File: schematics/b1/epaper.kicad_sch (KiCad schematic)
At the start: 11 parts

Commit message: Updated dates.
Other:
- title: B1 -> E-Paper
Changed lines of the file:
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@@
   (paper "A5")
   (title_block
-    (title "B1")
-    (date "2024-02-15")
+    (title "E-Paper")
+    (date "2024-02-19")
     (rev "1")
     (company "shawnd.xyz")

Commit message: Updated annotations.
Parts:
- renumbered TP48 to TP47, TP51 to TP48, TP50 to TP49, TP49 to TP50, TP47 to TP51, U6 to U8
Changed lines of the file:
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@@
   (symbol (lib_id "power:GND") (at 58.42 45.72 0) (unit 1)
     (in_bom yes) (on_board yes) (dnp no) (fields_autoplaced)
-    (property "Reference" "#PWR040" (at 58.42 52.07 0)
+    (property "Reference" "#PWR039" (at 58.42 52.07 0)
       (effects (font (size 1.27 1.27)) hide)
     )
@@
       (project "b1"
         (path "/d6142fa5-2354-4512-9919-37616259c364/793d8791-3733-41a0-9e62-38f7f458300f"
-          (reference "#PWR040") (unit 1)
+          (reference "#PWR039") (unit 1)
         )
       )
@@
   (symbol (lib_id "Connector:TestPoint") (at 74.93 76.2 180) (unit 1)
     (in_bom yes) (on_board yes) (dnp no)
-    (property "Reference" "TP51" (at 73.66 81.28 90)
+    (property "Reference" "TP48" (at 74.93 81.28 90)
       (effects (font (size 1.27 1.27)) (justify left))
     )
     (property "Value" "TestPoint" (at 76.2 81.28 90)
-      (effects (font (size 1.27 1.27)) (justify left))
+      (effects (font (size 1.27 1.27)) (justify left) hide)
     )
     (property "Footprint" "" (at 69.85 76.2 0)
@@
       (project "b1"
         (path "/d6142fa5-2354-4512-9919-37616259c364/793d8791-3733-41a0-9e62-38f7f458300f"
+          (reference "TP48") (unit 1)
+        )
+      )
+    )
+  )
+  (symbol (lib_id "Connector:TestPoint") (at 87.63 76.2 180) (unit 1)
+    (in_bom yes) (on_board yes) (dnp no)
+    (property "Reference" "TP50" (at 87.63 81.28 90)
+      (effects (font (size 1.27 1.27)) (justify left))
+    )
+    (property "Value" "TestPoint" (at 88.9 81.28 90)
+      (effects (font (size 1.27 1.27)) (justify left) hide)
+    )
+    (property "Footprint" "" (at 82.55 76.2 0)
+      (effects (font (size 1.27 1.27)) hide)
+    )
+    (property "Datasheet" "~" (at 82.55 76.2 0)
+      (effects (font (size 1.27 1.27)) hide)
+    )
+    (pin "1")
+    (instances
+      (project "b1"
+        (path "/d6142fa5-2354-4512-9919-37616259c364/793d8791-3733-41a0-9e62-38f7f458300f"
+          (reference "TP50") (unit 1)
+        )
+      )
+    )
+  )
+  (symbol (lib_id "Connector:TestPoint") (at 105.41 77.47 270) (unit 1)
+    (in_bom yes) (on_board yes) (dnp no)
+    (property "Reference" "TP51" (at 110.49 77.47 90)
+      (effects (font (size 1.27 1.27)) (justify left))
+    )
+    (property "Value" "TestPoint" (at 110.49 78.74 90)
+      (effects (font (size 1.27 1.27)) (justify left) hide)
+    )
+    (property "Footprint" "" (at 105.41 82.55 0)
+      (effects (font (size 1.27 1.27)) hide)
+    )
+    (property "Datasheet" "~" (at 105.41 82.55 0)
+      (effects (font (size 1.27 1.27)) hide)
+    )
+    (pin "1")
+    (instances
+      (project "b1"
+        (path "/d6142fa5-2354-4512-9919-37616259c364/793d8791-3733-41a0-9e62-38f7f458300f"
           (reference "TP51") (unit 1)
         )
@@
     )
   )
-  (symbol (lib_id "Connector:TestPoint") (at 87.63 76.2 180) (unit 1)
-    (in_bom yes) (on_board yes) (dnp no)
-    (property "Reference" "TP49" (at 86.36 81.28 90)
-      (effects (font (size 1.27 1.27)) (justify left))
-    )
-    (property "Value" "TestPoint" (at 88.9 81.28 90)
-      (effects (font (size 1.27 1.27)) (justify left))
-    )
-    (property "Footprint" "" (at 82.55 76.2 0)
-      (effects (font (size 1.27 1.27)) hide)
-    )
-    (property "Datasheet" "~" (at 82.55 76.2 0)
-      (effects (font (size 1.27 1.27)) hide)
-    )
-    (pin "1")
-    (instances
-      (project "b1"
-        (path "/d6142fa5-2354-4512-9919-37616259c364/793d8791-3733-41a0-9e62-38f7f458300f"
-          (reference "TP49") (unit 1)
-        )
-      )
-    )
-  )
-  (symbol (lib_id "Connector:TestPoint") (at 105.41 77.47 270) (unit 1)
-    (in_bom yes) (on_board yes) (dnp no) (fields_autoplaced)
-    (property "Reference" "TP47" (at 110.49 76.2 90)
-      (effects (font (size 1.27 1.27)) (justify left))
-    )
-    (property "Value" "TestPoint" (at 110.49 78.74 90)
-      (effects (font (size 1.27 1.27)) (justify left))
-    )
-    (property "Footprint" "" (at 105.41 82.55 0)
-      (effects (font (size 1.27 1.27)) hide)
-    )
-    (property "Datasheet" "~" (at 105.41 82.55 0)
+  (symbol (lib_id "Connector:TestPoint") (at 121.92 59.69 180) (unit 1)
+    (in_bom yes) (on_board yes) (dnp no)
+    (property "Reference" "TP47" (at 121.92 64.77 90)
+      (effects (font (size 1.27 1.27)) (justify left))
+    )
+    (property "Value" "TestPoint" (at 123.19 64.77 90)
+      (effects (font (size 1.27 1.27)) (justify left) hide)
+    )
+    (property "Footprint" "" (at 116.84 59.69 0)
+      (effects (font (size 1.27 1.27)) hide)
+    )
+    (property "Datasheet" "~" (at 116.84 59.69 0)
       (effects (font (size 1.27 1.27)) hide)
     )
@@
         (path "/d6142fa5-2354-4512-9919-37616259c364/793d8791-3733-41a0-9e62-38f7f458300f"
           (reference "TP47") (unit 1)
-        )
-      )
-    )
-  )
-  (symbol (lib_id "Connector:TestPoint") (at 121.92 59.69 180) (unit 1)
-    (in_bom yes) (on_board yes) (dnp no)
-    (property "Reference" "TP48" (at 120.65 64.77 90)
-      (effects (font (size 1.27 1.27)) (justify left))
-    )
-    (property "Value" "TestPoint" (at 123.19 64.77 90)
-      (effects (font (size 1.27 1.27)) (justify left))
-    )
-    (property "Footprint" "" (at 116.84 59.69 0)
-      (effects (font (size 1.27 1.27)) hide)
-    )
-    (property "Datasheet" "~" (at 116.84 59.69 0)
-      (effects (font (size 1.27 1.27)) hide)
-    )
-    (pin "1")
-    (instances
-      (project "b1"
-        (path "/d6142fa5-2354-4512-9919-37616259c364/793d8791-3733-41a0-9e62-38f7f458300f"
-          (reference "TP48") (unit 1)
         )
       )
@@
   (symbol (lib_id "power:GND") (at 104.14 78.74 0) (unit 1)
     (in_bom yes) (on_board yes) (dnp no) (fields_autoplaced)
-    (property "Reference" "#PWR021" (at 104.14 85.09 0)
+    (property "Reference" "#PWR040" (at 104.14 85.09 0)
       (effects (font (size 1.27 1.27)) hide)
     )
@@
       (project "b1"
         (path "/d6142fa5-2354-4512-9919-37616259c364/793d8791-3733-41a0-9e62-38f7f458300f"
-          (reference "#PWR021") (unit 1)
+          (reference "#PWR040") (unit 1)
         )
       )
@@
   (symbol (lib_id "custom:E-paper_Display") (at 104.14 58.42 0) (unit 1)
     (in_bom yes) (on_board yes) (dnp no)
-    (property "Reference" "U6" (at 106.68 49.53 0)
+    (property "Reference" "U8" (at 106.68 49.53 0)
       (effects (font (size 1.27 1.27)))
     )
@@
       (project "b1"
         (path "/d6142fa5-2354-4512-9919-37616259c364/793d8791-3733-41a0-9e62-38f7f458300f"
-          (reference "U6") (unit 1)
+          (reference "U8") (unit 1)
         )
       )
@@
   )
   (symbol (lib_id "Connector:TestPoint") (at 105.41 41.91 270) (unit 1)
-    (in_bom yes) (on_board yes) (dnp no) (fields_autoplaced)
-    (property "Reference" "TP46" (at 110.49 40.64 90)
+    (in_bom yes) (on_board yes) (dnp no)
+    (property "Reference" "TP46" (at 110.49 41.91 90)
       (effects (font (size 1.27 1.27)) (justify left))
     )
     (property "Value" "TestPoint" (at 110.49 43.18 90)
-      (effects (font (size 1.27 1.27)) (justify left))
+      (effects (font (size 1.27 1.27)) (justify left) hide)
     )
     (property "Footprint" "" (at 105.41 46.99 0)
@@
   (symbol (lib_id "Connector:TestPoint") (at 81.28 76.2 180) (unit 1)
     (in_bom yes) (on_board yes) (dnp no)
-    (property "Reference" "TP50" (at 80.01 81.28 90)
+    (property "Reference" "TP49" (at 81.28 81.28 90)
       (effects (font (size 1.27 1.27)) (justify left))
     )
     (property "Value" "TestPoint" (at 82.55 81.28 90)
-      (effects (font (size 1.27 1.27)) (justify left))
+      (effects (font (size 1.27 1.27)) (justify left) hide)
     )
     (property "Footprint" "" (at 76.2 76.2 0)
@@
       (project "b1"
         (path "/d6142fa5-2354-4512-9919-37616259c364/793d8791-3733-41a0-9e62-38f7f458300f"
-          (reference "TP50") (unit 1)
-        )
-      )
+          (reference "TP49") (unit 1)
+        )
+      )

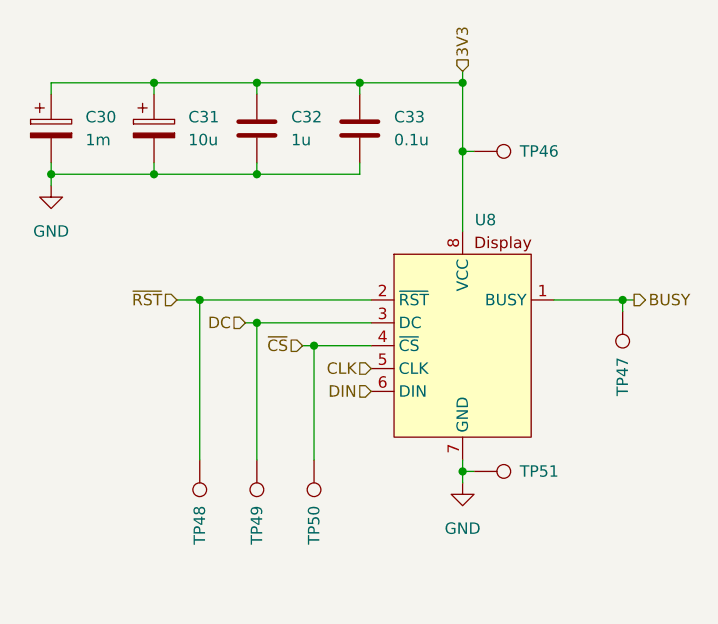
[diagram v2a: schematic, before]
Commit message: Tweaked wiring.
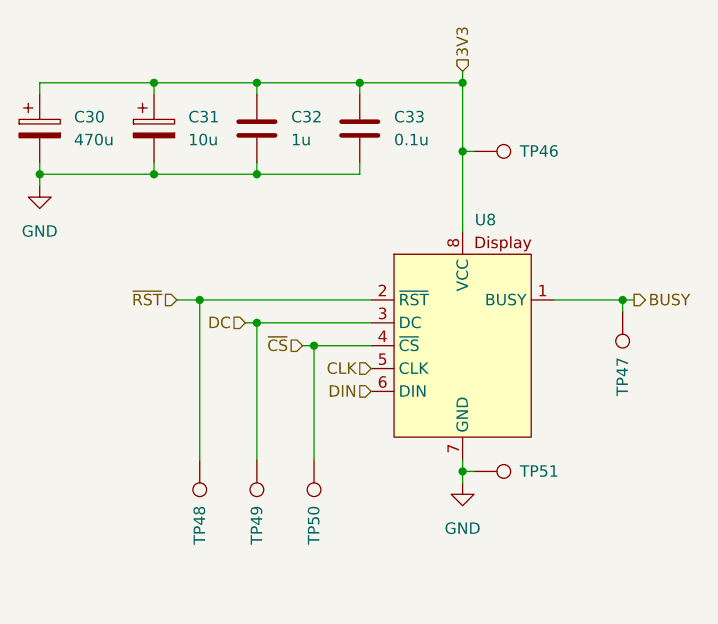
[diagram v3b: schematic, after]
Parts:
- C30: value 1m -> 470u
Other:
- moved on the sheet: C30
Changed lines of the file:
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@@
   (junction (at 104.14 77.47) (diameter 0) (color 0 0 0 0)
   )
-  (junction (at 58.42 44.45) (diameter 0) (color 0 0 0 0)
-  )
   (junction (at 104.14 34.29) (diameter 0) (color 0 0 0 0)
   )
+  (junction (at 57.15 44.45) (diameter 0) (color 0 0 0 0)
+  )
   (junction (at 69.85 34.29) (diameter 0) (color 0 0 0 0)
   )
@@
     (stroke (width 0) (type default))
   )
-  (wire (pts (xy 58.42 34.29) (xy 69.85 34.29))
+  (wire (pts (xy 57.15 34.29) (xy 69.85 34.29))
     (stroke (width 0) (type default))
   )
@@
     (stroke (width 0) (type default))
   )
-  (wire (pts (xy 58.42 45.72) (xy 58.42 44.45))
+  (wire (pts (xy 57.15 45.72) (xy 57.15 44.45))
     (stroke (width 0) (type default))
   )
@@
     (stroke (width 0) (type default))
   )
-  (wire (pts (xy 58.42 35.56) (xy 58.42 34.29))
+  (wire (pts (xy 57.15 35.56) (xy 57.15 34.29))
     (stroke (width 0) (type default))
   )
@@
     (stroke (width 0) (type default))
   )
-  (wire (pts (xy 58.42 44.45) (xy 69.85 44.45))
+  (wire (pts (xy 57.15 44.45) (xy 69.85 44.45))
     (stroke (width 0) (type default))
   )
@@
     (stroke (width 0) (type default))
   )
-  (wire (pts (xy 58.42 43.18) (xy 58.42 44.45))
+  (wire (pts (xy 57.15 43.18) (xy 57.15 44.45))
     (stroke (width 0) (type default))
   )
@@
     (effects (font (size 1.27 1.27)) (justify left))
   )
-  (symbol (lib_id "power:GND") (at 58.42 45.72 0) (unit 1)
+  (symbol (lib_id "power:GND") (at 57.15 45.72 0) (unit 1)
     (in_bom yes) (on_board yes) (dnp no) (fields_autoplaced)
-    (property "Reference" "#PWR039" (at 58.42 52.07 0)
-      (effects (font (size 1.27 1.27)) hide)
-    )
-    (property "Value" "GND" (at 58.42 50.8 0)
+    (property "Reference" "#PWR039" (at 57.15 52.07 0)
+      (effects (font (size 1.27 1.27)) hide)
+    )
+    (property "Value" "GND" (at 57.15 50.8 0)
       (effects (font (size 1.27 1.27)))
     )
-    (property "Footprint" "" (at 58.42 45.72 0)
-      (effects (font (size 1.27 1.27)) hide)
-    )
-    (property "Datasheet" "" (at 58.42 45.72 0)
+    (property "Footprint" "" (at 57.15 45.72 0)
+      (effects (font (size 1.27 1.27)) hide)
+    )
+    (property "Datasheet" "" (at 57.15 45.72 0)
       (effects (font (size 1.27 1.27)) hide)
     )
@@
     )
   )
-  (symbol (lib_id "Device:C_Polarized") (at 58.42 39.37 0) (unit 1)
-    (in_bom yes) (on_board yes) (dnp no)
-    (property "Reference" "C30" (at 62.23 38.1 0)
-      (effects (font (size 1.27 1.27)) (justify left))
-    )
-    (property "Value" "1m" (at 62.23 40.64 0)
-      (effects (font (size 1.27 1.27)) (justify left))
-    )
-    (property "Footprint" "" (at 59.3852 43.18 0)
-      (effects (font (size 1.27 1.27)) hide)
-    )
-    (property "Datasheet" "~" (at 58.42 39.37 0)
-      (effects (font (size 1.27 1.27)) hide)
-    )
+  (symbol (lib_id "Device:C_Polarized") (at 57.15 39.37 0) (unit 1)
+    (in_bom yes) (on_board yes) (dnp no)
+    (property "Reference" "C30" (at 60.96 38.1 0)
+      (effects (font (size 1.27 1.27)) (justify left))
+    )
+    (property "Value" "470u" (at 60.96 40.64 0)
+      (effects (font (size 1.27 1.27)) (justify left))
+    )
+    (property "Footprint" "" (at 58.1152 43.18 0)
+      (effects (font (size 1.27 1.27)) hide)
+    )
+    (property "Datasheet" "~" (at 57.15 39.37 0)
+      (effects (font (size 1.27 1.27)) hide)
+    )

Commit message: Assigned some footprints.
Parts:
- C30: footprint (none) -> Capacitor_THT:CP_Radial_D8.0mm_P3.80mm
- C31: footprint (none) -> Capacitor_THT:CP_Radial_D4.0mm_P2.00mm
- C32, C33: footprint (none) -> Capacitor_SMD:C_1206_3216Metric_Pad1.33x1.80mm_HandSolder
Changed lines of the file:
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@@
       (effects (font (size 1.27 1.27)) (justify left))
     )
-    (property "Footprint" "" (at 82.2452 43.18 0)
+    (property "Footprint" "Capacitor_SMD:C_1206_3216Metric_Pad1.33x1.80mm_HandSolder" (at 82.2452 43.18 0)
       (effects (font (size 1.27 1.27)) hide)
     )
@@
       (effects (font (size 1.27 1.27)) (justify left))
     )
-    (property "Footprint" "" (at 93.6752 43.18 0)
+    (property "Footprint" "Capacitor_SMD:C_1206_3216Metric_Pad1.33x1.80mm_HandSolder" (at 93.6752 43.18 0)
       (effects (font (size 1.27 1.27)) hide)
     )
@@
       (effects (font (size 1.27 1.27)) (justify left))
     )
-    (property "Footprint" "" (at 70.8152 43.18 0)
+    (property "Footprint" "Capacitor_THT:CP_Radial_D4.0mm_P2.00mm" (at 70.8152 43.18 0)
       (effects (font (size 1.27 1.27)) hide)
     )
@@
       (effects (font (size 1.27 1.27)) (justify left))
     )
-    (property "Footprint" "" (at 58.1152 43.18 0)
+    (property "Footprint" "Capacitor_THT:CP_Radial_D8.0mm_P3.80mm" (at 58.1152 43.18 0)
       (effects (font (size 1.27 1.27)) hide)
     )

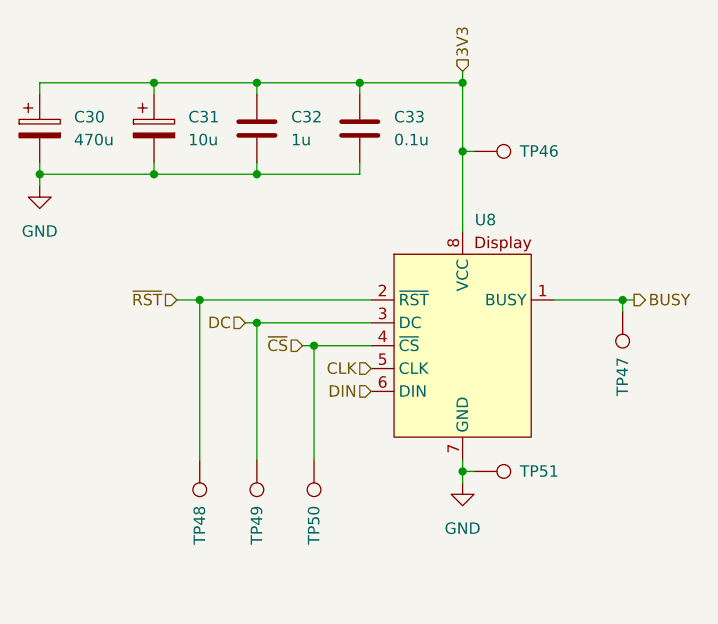
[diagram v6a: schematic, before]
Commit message: Finished assigning footprints.
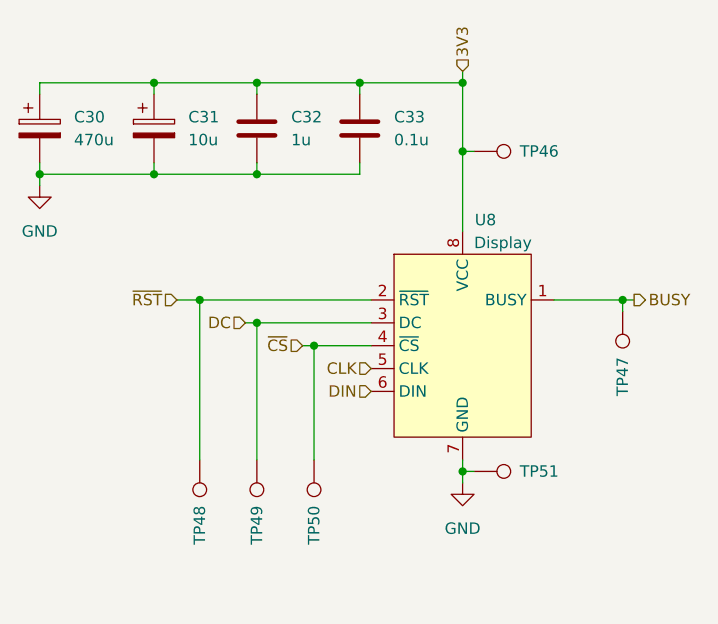
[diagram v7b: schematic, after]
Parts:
- TP46, TP47, TP48, TP49, TP50, TP51: footprint (none) -> TestPoint:TestPoint_Loop_D2.50mm_Drill1.0mm
- U8: value ~ -> Display; footprint (none) -> Connector_PinHeader_2.00mm:PinHeader_1x08_P2.00mm_Horizontal
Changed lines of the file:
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@@
       (effects (font (size 1.27 1.27)) (justify left) hide)
     )
-    (property "Footprint" "" (at 69.85 76.2 0)
+    (property "Footprint" "TestPoint:TestPoint_Loop_D2.50mm_Drill1.0mm" (at 69.85 76.2 0)
       (effects (font (size 1.27 1.27)) hide)
     )
@@
       (effects (font (size 1.27 1.27)) (justify left) hide)
     )
-    (property "Footprint" "" (at 82.55 76.2 0)
+    (property "Footprint" "TestPoint:TestPoint_Loop_D2.50mm_Drill1.0mm" (at 82.55 76.2 0)
       (effects (font (size 1.27 1.27)) hide)
     )
@@
       (effects (font (size 1.27 1.27)) (justify left) hide)
     )
-    (property "Footprint" "" (at 105.41 82.55 0)
+    (property "Footprint" "TestPoint:TestPoint_Loop_D2.50mm_Drill1.0mm" (at 105.41 82.55 0)
       (effects (font (size 1.27 1.27)) hide)
     )
@@
       (effects (font (size 1.27 1.27)) (justify left) hide)
     )
-    (property "Footprint" "" (at 116.84 59.69 0)
+    (property "Footprint" "TestPoint:TestPoint_Loop_D2.50mm_Drill1.0mm" (at 116.84 59.69 0)
       (effects (font (size 1.27 1.27)) hide)
     )
@@
       (effects (font (size 1.27 1.27)))
     )
-    (property "Value" "~" (at 104.14 50.8 0)
-      (effects (font (size 1.27 1.27)))
-    )
-    (property "Footprint" "" (at 104.14 50.8 0)
+    (property "Value" "Display" (at 105.41 52.07 0)
+      (effects (font (size 1.27 1.27)) (justify left))
+    )
+    (property "Footprint" "Connector_PinHeader_2.00mm:PinHeader_1x08_P2.00mm_Horizontal" (at 104.14 50.8 0)
       (effects (font (size 1.27 1.27)) hide)
     )
@@
       (effects (font (size 1.27 1.27)) (justify left) hide)
     )
-    (property "Footprint" "" (at 105.41 46.99 0)
+    (property "Footprint" "TestPoint:TestPoint_Loop_D2.50mm_Drill1.0mm" (at 105.41 46.99 0)
       (effects (font (size 1.27 1.27)) hide)
     )
@@
       (effects (font (size 1.27 1.27)) (justify left) hide)
     )
-    (property "Footprint" "" (at 76.2 76.2 0)
-      (effects (font (size 1.27 1.27)) hide)
-    )
+    (property "Footprint" "TestPoint:TestPoint_Loop_D2.50mm_Drill1.0mm" (at 76.2 76.2 0)
+      (effects (font (size 1.27 1.27)) hide)
+    )
